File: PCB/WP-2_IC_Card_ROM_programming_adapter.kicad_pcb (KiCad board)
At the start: 2 copper layers, 17.8 x 49.5 mm, 3 parts, among them J1 Conn_01x38_Male, J2 Conn_02x16_Counter_Clockwise

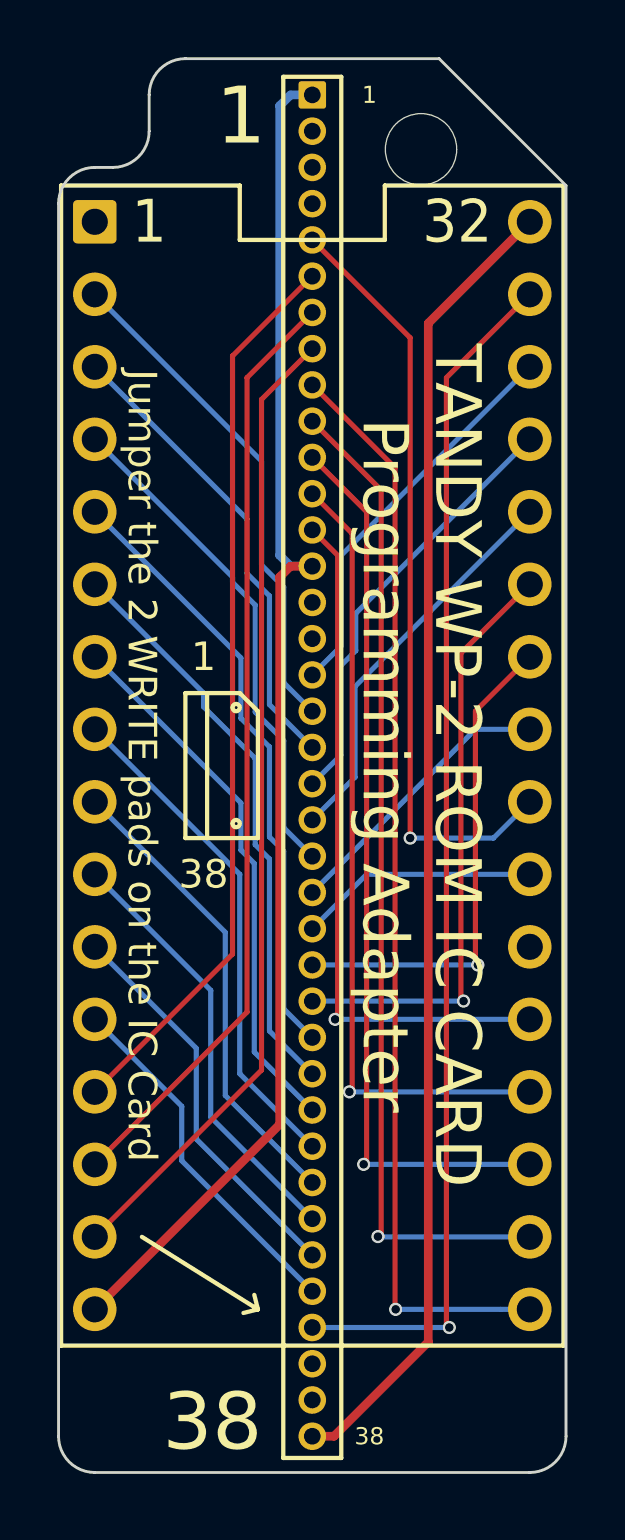
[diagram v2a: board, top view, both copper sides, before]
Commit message: more clean up from ditching the small boards
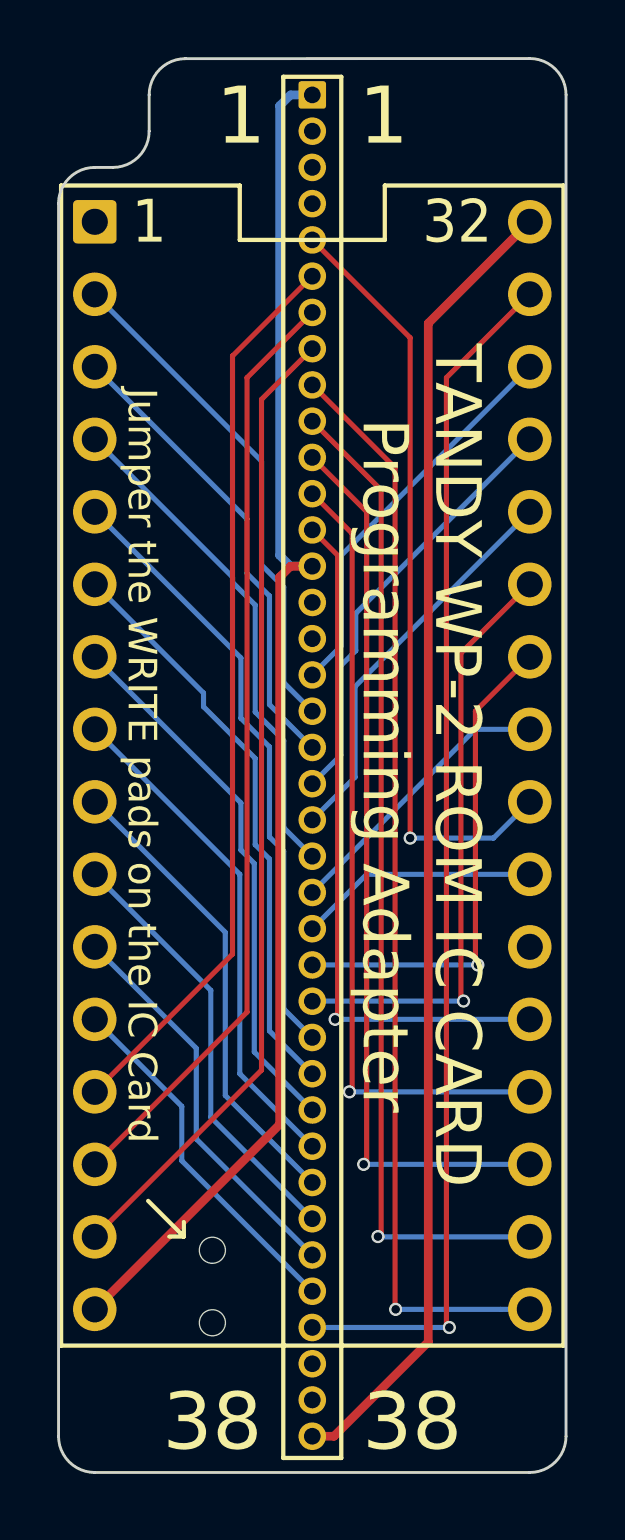
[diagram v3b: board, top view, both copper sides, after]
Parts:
- removed the REF** at (143.5, 78.1)
- added REF**: , 0_LOCAL:JP2_npth_storage, F.Cu at (136.2, 117.9)
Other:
- outline, holes or cut-outs redrawn
- board text added: "Jumper the WRITE pads on the IC Card"
- board text added: "WP-2_IC_Card_ROM_programming_adapter v002"
- board text removed: "Jumper the 2 WRITE pads on the IC Card"
- board text removed: "WP-2_IC_Card_ROM_programming_adapter v001"
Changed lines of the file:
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@@
   (general
     (thickness 1.6)
-    (drawings 58)
+    (drawings 48)
     (tracks 141)
     (zones 0)
@@
   (title_block
     (title "Programming Adapter for WP-2 IC Card")
-    (date 2020-10-29)
+    (date 2020-11-16)
+    (rev 002)
+    (company "Brian K. White - b.kenyon.w@gmail.com")
   )
   (layers
@@
     (add_net /~OE)
     (add_net GND)
+  )
+  (module 0_LOCAL:JP2_npth_storage (layer F.Cu)
+    (at 136.186 117.945 90)
+    (fp_text reference REF** (at 0 -1.25 -90 unlocked) (layer F.SilkS) hide
+      (effects (font (size 0.8128 0.8128) (thickness 0.0762)))
+    )
+    (fp_text value "" (at 0 -2 90) (layer F.Fab) hide
+      (effects (font (size 0.8128 0.8128) (thickness 0.0254)))
+    )
+    (pad "" np_thru_hole circle (at 1.27 0 90) (size 0.9144 0.9144) (drill 0.9144) (layers *.Cu))
+    (pad "" np_thru_hole circle (at -1.27 0 90) (size 0.9144 0.9144) (drill 0.9144) (layers *.Cu))
   )
   (module 0_LOCAL:Pin_Header_Straight_1x38_Pitch1.27mm (layer F.Cu)
@@
       (rotate (xyz 0 0 0))
     )
-    (model ${KIPRJMOD}/WP-2_IC_Card_v003_ROM_assembly.step_x
-      (offset (xyz -1.1303 0 9.499599999999999))
-      (scale (xyz 1 1 1))
-      (rotate (xyz 0 -90 0))
-    )
-    (model ${KIPRJMOD}/WP-2_IC_Card_ROM_carried.step_x
-      (offset (xyz -1.1303 0 9.499599999999999))
-      (scale (xyz 1 1 1))
-      (rotate (xyz 0 -90 0))
-    )
-    (model ${KIPRJMOD}/WP-2_IC_Card_ROM_no_carrier.step_x
+    (model ${KIPRJMOD}/WP-2_IC_Card_ROM.step
       (offset (xyz -1.1303 0 9.499599999999999))
       (scale (xyz 1 1 1))
@@
     )
   )
-  (module MountingHole:MountingHole_2.5mm (layer F.Cu)
-    (at 143.496 78.105)
-    (descr "Mounting Hole 2.5mm, no annular")
-    (tags "mounting hole 2.5mm no annular")
-    (attr virtual)
-    (fp_text reference REF** (at 0 -3.5) (layer F.SilkS) hide
-      (effects (font (size 1 1) (thickness 0.15)))
-    )
-    (fp_text value MountingHole_2.5mm (at 0 3.5) (layer F.Fab)
-      (effects (font (size 1 1) (thickness 0.15)))
-    )
-    (fp_circle (center 0 0) (end 2.5 0) (layer Cmts.User) (width 0.15))
-    (fp_circle (center 0 0) (end 2.75 0) (layer F.CrtYd) (width 0.05))
-    (fp_text user %R (at 0.3 0) (layer F.Fab)
-      (effects (font (size 1 1) (thickness 0.15)))
-    )
-    (pad 1 np_thru_hole circle (at 0 0) (size 2.5 2.5) (drill 2.5) (layers *.Cu *.Mask))
-  )
+  (gr_text 38 (at 143.186 122.695) (layer F.SilkS)
+    (effects (font (size 2 2) (thickness 0.4)))
+  )
+  (gr_text 1 (at 142.186 76.945) (layer F.SilkS)
+    (effects (font (size 2 2) (thickness 0.4)))
+  )
+  (gr_arc (start 147.306 76.195) (end 148.576 76.195) (angle -90) (layer Edge.Cuts) (width 0.1))
   (gr_text "CENTER PINS OTHER SIDE" (at 138.186 99.695 90) (layer B.SilkS)
     (effects (font (size 1 1) (thickness 0.15)) (justify mirror))
   )
-  (gr_text "WP-2_IC_Card_ROM_programming_adapter v001" (at 143.186 99.695 90) (layer B.SilkS)
+  (gr_text "WP-2_IC_Card_ROM_programming_adapter v002" (at 143.186 99.695 90) (layer B.SilkS)
     (effects (font (size 1 1) (thickness 0.1)) (justify mirror))
-  )
-  (gr_line (start 148.576 79.375) (end 144.131 74.93) (layer Edge.Cuts) (width 0.1))
-  (gr_text 38 (at 141.686 123.195) (layer F.SilkS)
-    (effects (font (size 0.6 0.6) (thickness 0.1)))
-  )
-  (gr_text 1 (at 141.686 76.2) (layer F.SilkS)
-    (effects (font (size 0.6 0.6) (thickness 0.1)))
   )
   (gr_line (start 138.67 75.565) (end 140.702 75.565) (layer F.SilkS) (width 0.15))
@@
     (effects (font (size 1.5 1.4) (thickness 0.2)))
   )
-  (gr_line (start 137.781 118.745) (end 137.273 118.872) (layer F.SilkS) (width 0.15))
-  (gr_line (start 137.654 118.237) (end 137.781 118.745) (layer F.SilkS) (width 0.15))
+  (gr_line (start 135.186 116.195) (end 134.678 116.195) (layer F.SilkS) (width 0.15))
+  (gr_line (start 135.186 115.687) (end 135.186 116.195) (layer F.SilkS) (width 0.15))
   (gr_line (start 148.486 120.015) (end 148.486 79.375) (layer F.SilkS) (width 0.15))
   (gr_line (start 130.886 120.015) (end 148.486 120.015) (layer F.SilkS) (width 0.15))
@@
     (effects (font (size 1.6 1.6) (thickness 0.2)))
   )
-  (gr_line (start 133.717 116.205) (end 137.781 118.745) (layer F.SilkS) (width 0.15))
-  (gr_text "Jumper the 2 WRITE pads on the IC Card" (at 133.717 99.695 -90) (layer F.SilkS)
+  (gr_line (start 133.936 114.945) (end 135.186 116.195) (layer F.SilkS) (width 0.15))
+  (gr_text "Jumper the WRITE pads on the IC Card" (at 133.717 99.695 -90) (layer F.SilkS)
     (effects (font (size 1 1) (thickness 0.15)))
-  )
-  (gr_text 38 (at 135.876 103.505) (layer F.SilkS)
-    (effects (font (size 1 1) (thickness 0.2)))
-  )
-  (gr_text 1 (at 135.876 95.885) (layer F.SilkS)
-    (effects (font (size 1 1) (thickness 0.2)))
   )
   (gr_text 38 (at 136.186 122.695) (layer F.SilkS)
@@
     (effects (font (size 2 2) (thickness 0.4)))
   )
-  (gr_circle (center 137.019 101.727) (end 137.019 101.854) (layer F.SilkS) (width 0.15))
-  (gr_circle (center 137.019 97.663) (end 137.019 97.79) (layer F.SilkS) (width 0.15))
-  (gr_line (start 136.003 102.235) (end 136.003 97.155) (layer F.SilkS) (width 0.15))
-  (gr_line (start 137.146 97.155) (end 135.241 97.155) (layer F.SilkS) (width 0.15))
-  (gr_line (start 137.781 97.79) (end 137.146 97.155) (layer F.SilkS) (width 0.15))
-  (gr_line (start 137.781 102.235) (end 137.781 97.79) (layer F.SilkS) (width 0.15))
-  (gr_line (start 135.241 102.235) (end 137.781 102.235) (layer F.SilkS) (width 0.15))
-  (gr_line (start 135.241 97.155) (end 135.241 102.235) (layer F.SilkS) (width 0.15))
   (gr_text "Programming Adapter" (at 142.226 99.695 -90) (layer F.SilkS)
     (effects (font (size 1.6 1.6) (thickness 0.2)))
@@
   (gr_line (start 133.971 77.47) (end 133.971 76.2) (layer Edge.Cuts) (width 0.1))
   (gr_line (start 132.066 78.74) (end 132.701 78.74) (layer Edge.Cuts) (width 0.1))
-  (gr_line (start 144.131 74.93) (end 135.241 74.93) (layer Edge.Cuts) (width 0.1))
-  (gr_line (start 148.576 123.19) (end 148.576 79.375) (layer Edge.Cuts) (width 0.1))
+  (gr_line (start 147.306 74.925) (end 135.241 74.93) (layer Edge.Cuts) (width 0.1))
+  (gr_line (start 148.576 123.19) (end 148.576 76.2) (layer Edge.Cuts) (width 0.1))
   (gr_line (start 132.066 124.46) (end 147.306 124.46) (layer Edge.Cuts) (width 0.1))
   (gr_line (start 130.796 80.01) (end 130.796 123.19) (layer Edge.Cuts) (width 0.1))

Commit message: missing /CE1 on programming adapter
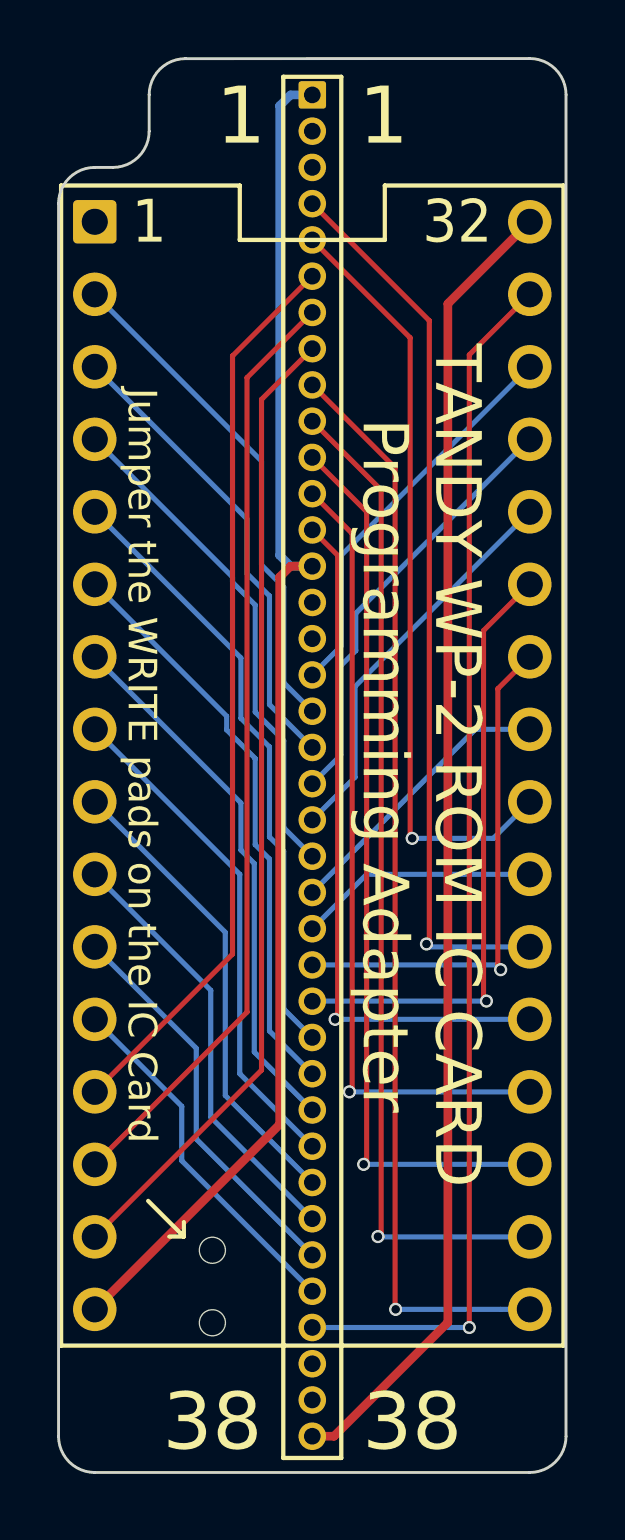
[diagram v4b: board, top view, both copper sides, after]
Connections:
- J1 pad 4: (no net) -> /~CE1
- J2 pad 22: (no net) -> /~CE1
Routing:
- net /~CE1: track 0.00 -> 31.3 mm, vias 0 -> 1
- net /A9: track 17.4 -> 18.1 mm
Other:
- net class Default: trace_width 0.16 -> 0.18; via_dia 0.41 -> 0.46; via_drill 0.25 -> 0.3
